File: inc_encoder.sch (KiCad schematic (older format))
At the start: 14 parts, among them U3 AM26LV32xD

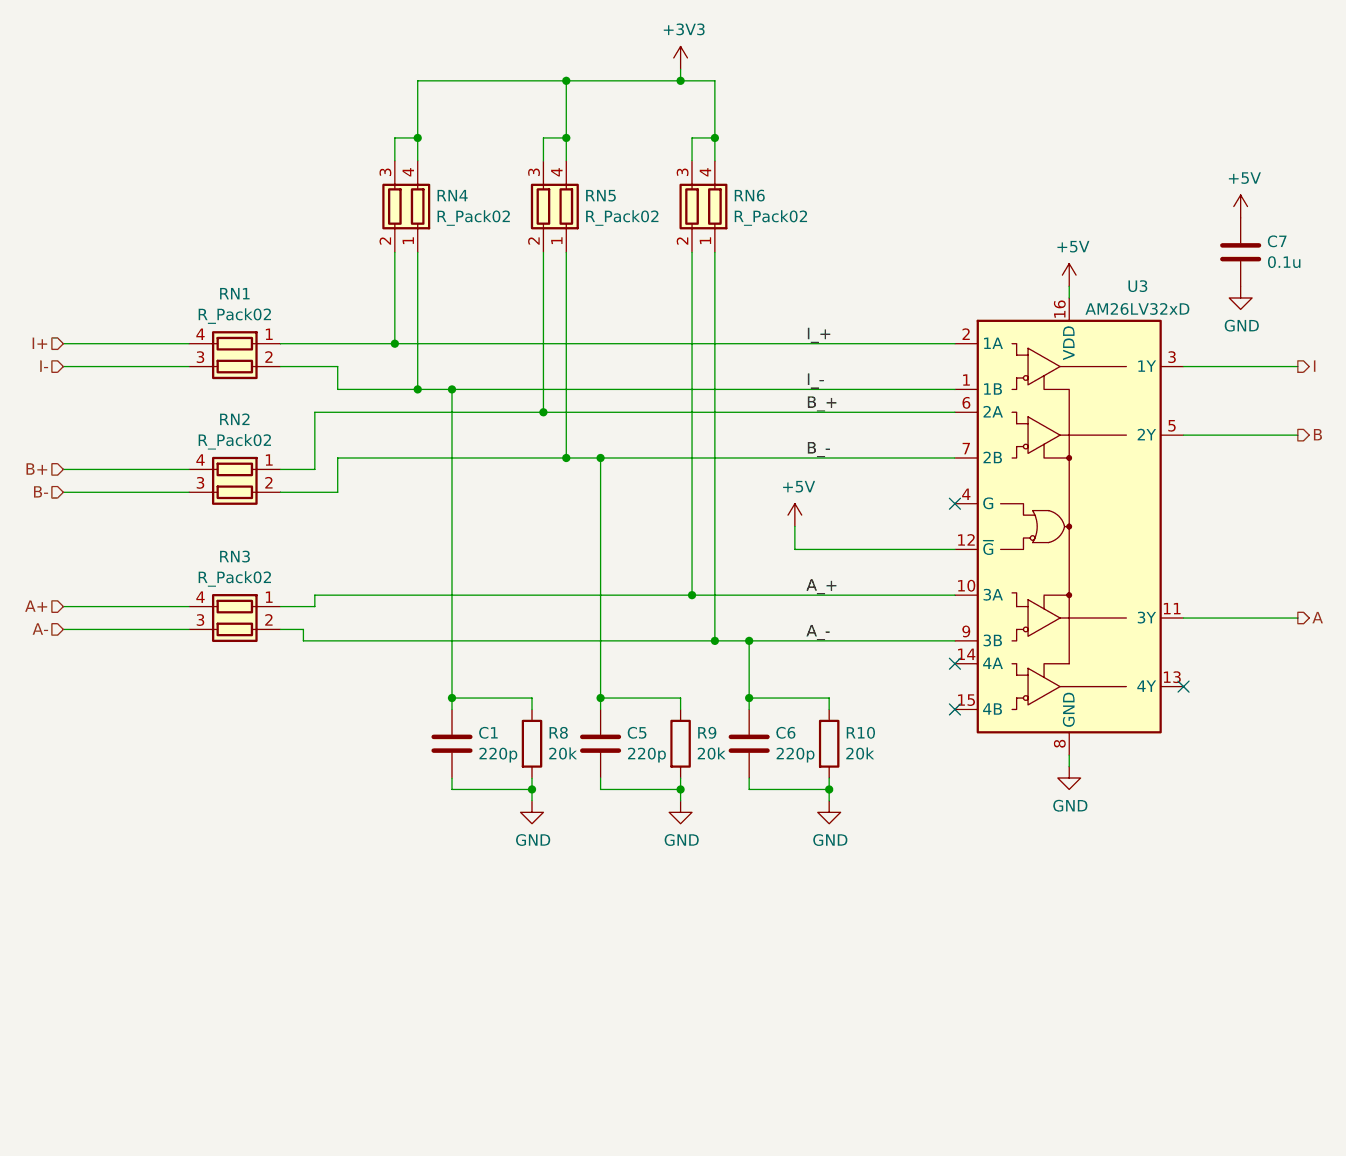
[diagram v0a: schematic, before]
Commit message: 見つけた設計ミスを全部反映
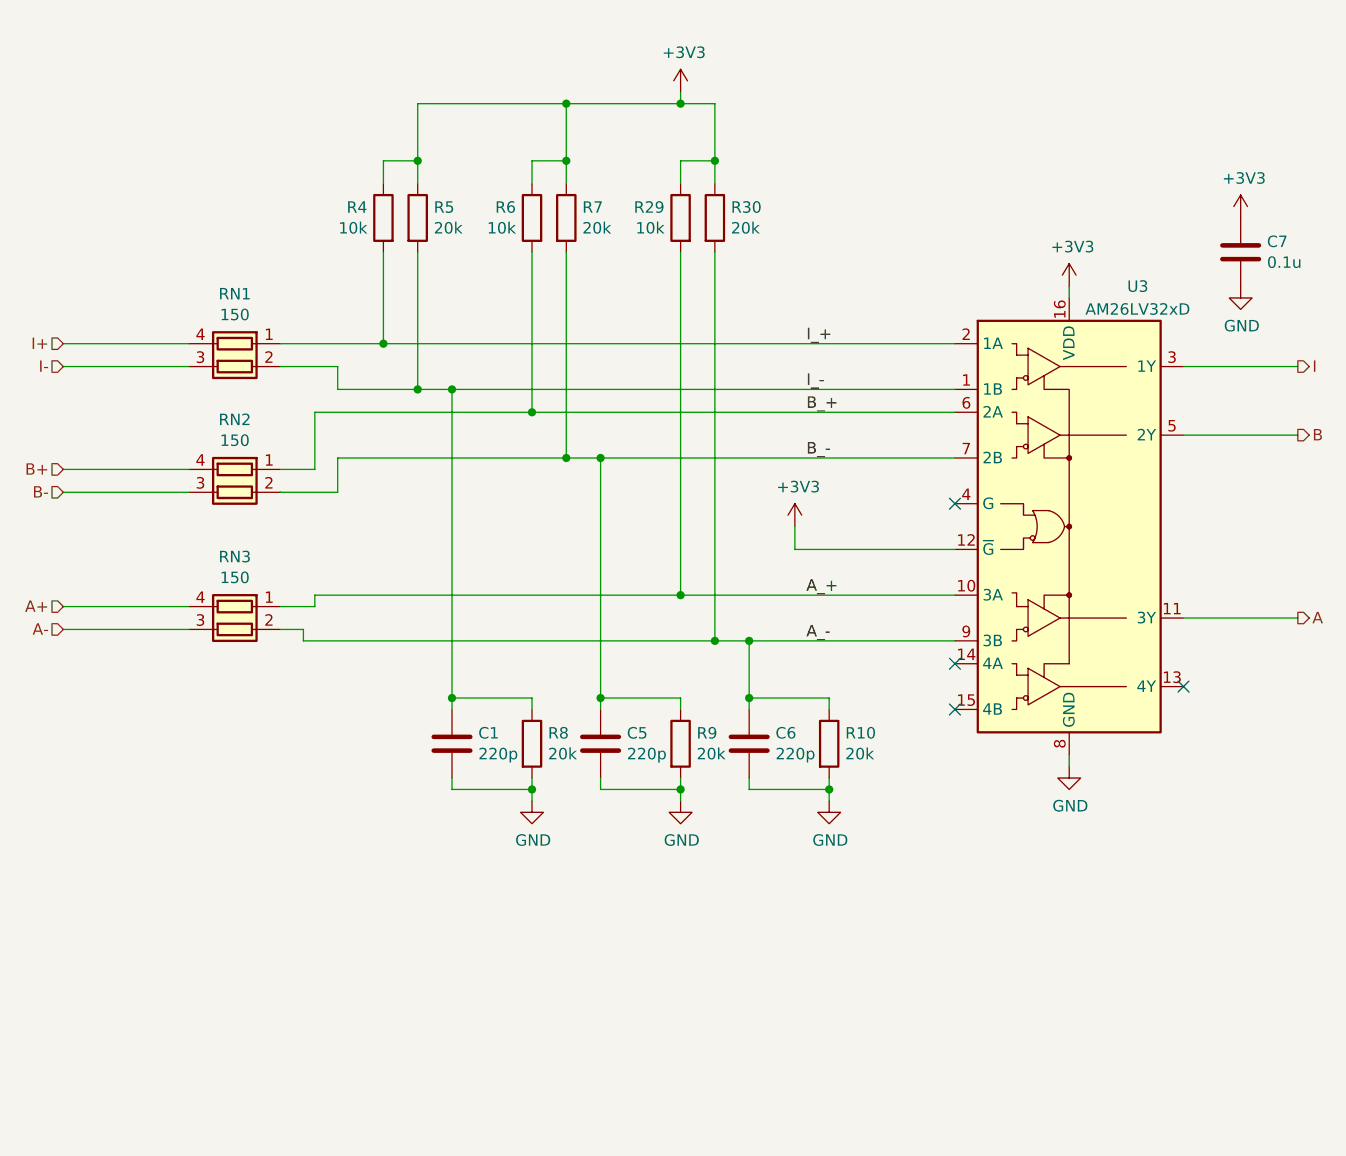
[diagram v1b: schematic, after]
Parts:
- removed RN4, RN5, RN6: R_Pack02, Resistor_SMD:R_Array_Concave_2x0603, symbol Device:R_Pack02
- added R29, R4, R6: 10k, Resistor_SMD:R_0603_1608Metric, symbol Device:R
- added R30, R5, R7: 20k, Resistor_SMD:R_0603_1608Metric, symbol Device:R
- RN1, RN2, RN3: value R_Pack02 -> 150
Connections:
- net +5V is gone; now on net +3V3: C7.1, U3.12 (~G), U3.16 (VDD)
- net +3V3: now also R29.1, R30.1, R4.1, R5.1, R6.1, R7.1
- net A_+: now also R29.2
- net A_-: now also R30.2
- net B_+: now also R6.2
- net B_-: now also R7.2
- net I_+: now also R4.2
- net I_-: now also R5.2
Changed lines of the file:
@@
 EESchema Schematic File Version 4
-LIBS:Encoder_check-cache
 EELAYER 30 0
 EELAYER END
@@
 NoConn ~ 5900 4800
 NoConn ~ 5900 5000
-$Comp
-L power:+5V #PWR?
-U 1 1 5E355A9E
-P 5200 4200
-AR Path="/5E355A9E" Ref="#PWR?"  Part="1"
-AR Path="/5E34E778/5E355A9E" Ref="#PWR0105"  Part="1"
-F 0 "#PWR0105" H 5200 4050 50  0001 C CNN
-F 1 "+5V" H 5215 4373 50  0000 C CNN
-F 2 "" H 5200 4200 50  0001 C CNN
-F 3 "" H 5200 4200 50  0001 C CNN
-	1    5200 4200
-	1    0    0    -1
-$EndComp
 Wire Wire Line
 	5200 4200 5200 4300
 Wire Wire Line
 	5200 4300 5900 4300
-$Comp
-L power:+5V #PWR?
-U 1 1 5E355AA6
-P 6400 3150
-AR Path="/5E355AA6" Ref="#PWR?"  Part="1"
-AR Path="/5E34E778/5E355AA6" Ref="#PWR0106"  Part="1"
-F 0 "#PWR0106" H 6400 3000 50  0001 C CNN
-F 1 "+5V" H 6415 3323 50  0000 C CNN
-F 2 "" H 6400 3150 50  0001 C CNN
-F 3 "" H 6400 3150 50  0001 C CNN
-	1    6400 3150
-	1    0    0    -1
-$EndComp
 Wire Wire Line
 	6400 3150 6400 3200
@@
 $EndComp
 $Comp
-L power:+5V #PWR?
-U 1 1 5E355AB3
-P 7150 2850
-AR Path="/5E355AB3" Ref="#PWR?"  Part="1"
-AR Path="/5E34E778/5E355AB3" Ref="#PWR0107"  Part="1"
-F 0 "#PWR0107" H 7150 2700 50  0001 C CNN
-F 1 "+5V" H 7165 3023 50  0000 C CNN
-F 2 "" H 7150 2850 50  0001 C CNN
-F 3 "" H 7150 2850 50  0001 C CNN
-	1    7150 2850
-	1    0    0    -1
-$EndComp
-$Comp
 L power:GND #PWR?
 U 1 1 5E355AB9
@@
 L power:+3V3 #PWR0122
 U 1 1 5E365891
-P 4700 2200
-F 0 "#PWR0122" H 4700 2050 50  0001 C CNN
-F 1 "+3V3" H 4715 2373 50  0000 C CNN
-F 2 "" H 4700 2200 50  0001 C CNN
-F 3 "" H 4700 2200 50  0001 C CNN
-	1    4700 2200
-	1    0    0    -1
-$EndComp
-Wire Wire Line
-	4700 2200 4700 2250
-Wire Wire Line
-	4700 2250 4850 2250
-Wire Wire Line
-	4850 2250 4850 2500
-Wire Wire Line
-	4750 2600 4750 2500
-Wire Wire Line
-	4750 2500 4850 2500
-Connection ~ 4850 2500
-Wire Wire Line
-	4850 2500 4850 2600
-Wire Wire Line
-	4700 2250 4200 2250
-Wire Wire Line
-	4200 2250 4200 2500
-Connection ~ 4700 2250
-Wire Wire Line
-	4200 2500 4100 2500
-Connection ~ 4200 2500
-Wire Wire Line
-	4200 2500 4200 2600
-Wire Wire Line
-	4100 2600 4100 2500
+P 4700 2300
+F 0 "#PWR0122" H 4700 2150 50  0001 C CNN
+F 1 "+3V3" H 4715 2473 50  0000 C CNN
+F 2 "" H 4700 2300 50  0001 C CNN
+F 3 "" H 4700 2300 50  0001 C CNN
+	1    4700 2300
+	1    0    0    -1
+$EndComp
+Wire Wire Line
+	4700 2300 4700 2350
+Wire Wire Line
+	4700 2350 4850 2350
+Wire Wire Line
+	4850 2350 4850 2600
+Wire Wire Line
+	4700 2700 4700 2600
+Wire Wire Line
+	4700 2600 4850 2600
+Connection ~ 4850 2600
+Wire Wire Line
+	4850 2600 4850 2700
+Wire Wire Line
+	4700 2350 4200 2350
+Wire Wire Line
+	4200 2350 4200 2600
+Connection ~ 4700 2350
+Wire Wire Line
+	4200 2600 4050 2600
+Connection ~ 4200 2600
+Wire Wire Line
+	4200 2600 4200 2700
+Wire Wire Line
+	4050 2700 4050 2600
 $Comp
 L Device:R R10
@@
 	4350 3900 5900 3900
 Wire Wire Line
-	2950 3400 3450 3400
+	2950 3400 3400 3400
 Wire Wire Line
 	3700 3600 3550 3600
 Wire Wire Line
-	3100 3700 4100 3700
-Wire Wire Line
-	3450 3000 3450 3400
-Connection ~ 3450 3400
-Wire Wire Line
-	3450 3400 5900 3400
+	3100 3700 4050 3700
+Wire Wire Line
+	3400 3000 3400 3400
+Connection ~ 3400 3400
+Wire Wire Line
+	3400 3400 5900 3400
 Wire Wire Line
 	3550 3000 3550 3600
 Connection ~ 3550 3600
 Wire Wire Line
-	4100 3000 4100 3700
-Connection ~ 4100 3700
-Wire Wire Line
-	4100 3700 5900 3700
+	4050 3000 4050 3700
+Connection ~ 4050 3700
+Wire Wire Line
+	4050 3700 5900 3700
 Wire Wire Line
 	4200 3000 4200 3900
@@
 Wire Wire Line
 	3100 4550 3100 4500
-$Comp
-L Device:R_Pack02 RN6
-U 1 1 5E4869DA
-P 4750 2800
-F 0 "RN6" H 4570 2846 50  0000 R CNN
-F 1 "R_Pack02" H 4570 2755 50  0000 R CNN
-F 2 "Resistor_SMD:R_Array_Concave_2x0603" V 4925 2800 50  0001 C CNN
-F 3 "~" H 4750 2800 50  0001 C CNN
-	1    4750 2800
-	-1   0    0    -1
-$EndComp
 $Comp
 L Device:R_Pack02 RN3
@@
 P 2750 4650
 F 0 "RN3" V 2433 4650 50  0000 C CNN
-F 1 "R_Pack02" V 2524 4650 50  0000 C CNN
+F 1 "150" V 2524 4650 50  0000 C CNN
 F 2 "Resistor_SMD:R_Array_Concave_2x0603" V 2925 4650 50  0001 C CNN
 F 3 "~" H 2750 4650 50  0001 C CNN
@@
 	0    -1   1    0
 $EndComp
-$Comp
-L Device:R_Pack02 RN5
-U 1 1 5E48D078
-P 4100 2800
-F 0 "RN5" H 3920 2846 50  0000 R CNN
-F 1 "R_Pack02" H 3920 2755 50  0000 R CNN
-F 2 "Resistor_SMD:R_Array_Concave_2x0603" V 4275 2800 50  0001 C CNN
-F 3 "~" H 4100 2800 50  0001 C CNN
-	1    4100 2800
-	-1   0    0    -1
-$EndComp
-$Comp
-L Device:R_Pack02 RN4
-U 1 1 5E48D4FD
-P 3450 2800
-F 0 "RN4" H 3270 2846 50  0000 R CNN
-F 1 "R_Pack02" H 3270 2755 50  0000 R CNN
-F 2 "Resistor_SMD:R_Array_Concave_2x0603" V 3625 2800 50  0001 C CNN
-F 3 "~" H 3450 2800 50  0001 C CNN
-	1    3450 2800
-	-1   0    0    -1
-$EndComp
-Wire Wire Line
-	3450 2600 3450 2500
-Wire Wire Line
-	3450 2500 3550 2500
-Wire Wire Line
-	3550 2500 3550 2600
-Wire Wire Line
-	3550 2500 3550 2250
-Wire Wire Line
-	3550 2250 4200 2250
-Connection ~ 3550 2500
-Connection ~ 4200 2250
+Wire Wire Line
+	3400 2700 3400 2600
+Wire Wire Line
+	3400 2600 3550 2600
+Wire Wire Line
+	3550 2600 3550 2700
+Wire Wire Line
+	3550 2600 3550 2350
+Wire Wire Line
+	3550 2350 4200 2350
+Connection ~ 3550 2600
+Connection ~ 4200 2350
 Wire Wire Line
 	3700 3600 5900 3600
@@
 P 2750 3500
 F 0 "RN1" V 2433 3500 50  0000 C CNN
-F 1 "R_Pack02" V 2524 3500 50  0000 C CNN
+F 1 "150" V 2524 3500 50  0000 C CNN
 F 2 "Resistor_SMD:R_Array_Concave_2x0603" V 2925 3500 50  0001 C CNN
 F 3 "~" H 2750 3500 50  0001 C CNN
@@
 P 2750 4050
 F 0 "RN2" V 2433 4050 50  0000 C CNN
-F 1 "R_Pack02" V 2524 4050 50  0000 C CNN
+F 1 "150" V 2524 4050 50  0000 C CNN
 F 2 "Resistor_SMD:R_Array_Concave_2x0603" V 2925 4050 50  0001 C CNN
 F 3 "~" H 2750 4050 50  0001 C CNN
@@
 	3050 4700 4850 4700
 Wire Wire Line
-	3100 4500 4750 4500
-Wire Wire Line
-	4750 3000 4750 4500
-Connection ~ 4750 4500
-Wire Wire Line
-	4750 4500 5900 4500
+	3100 4500 4700 4500
+Wire Wire Line
+	4700 3000 4700 4500
+Connection ~ 4700 4500
+Wire Wire Line
+	4700 4500 5900 4500
 Wire Wire Line
 	4850 3000 4850 4700
@@
 Text Label 5250 3400 0    50   ~ 0
 I_+
+$Comp
+L Device:R R30
+U 1 1 5E55B2E2
+P 4850 2850
+F 0 "R30" H 4920 2896 50  0000 L CNN
+F 1 "20k" H 4920 2805 50  0000 L CNN
+F 2 "Resistor_SMD:R_0603_1608Metric" V 4780 2850 50  0001 C CNN
+F 3 "~" H 4850 2850 50  0001 C CNN
+	1    4850 2850
+	1    0    0    -1
+$EndComp
+$Comp
+L Device:R R7
+U 1 1 5E55BC17
+P 4200 2850
+F 0 "R7" H 4270 2896 50  0000 L CNN
+F 1 "20k" H 4270 2805 50  0000 L CNN
+F 2 "Resistor_SMD:R_0603_1608Metric" V 4130 2850 50  0001 C CNN
+F 3 "~" H 4200 2850 50  0001 C CNN
+	1    4200 2850
+	1    0    0    -1
+$EndComp
+$Comp
+L Device:R R5
+U 1 1 5E55BEC8
+P 3550 2850
+F 0 "R5" H 3620 2896 50  0000 L CNN
+F 1 "20k" H 3620 2805 50  0000 L CNN
+F 2 "Resistor_SMD:R_0603_1608Metric" V 3480 2850 50  0001 C CNN
+F 3 "~" H 3550 2850 50  0001 C CNN
+	1    3550 2850
+	1    0    0    -1
+$EndComp
+$Comp
+L Device:R R29
+U 1 1 5E55C33C
+P 4700 2850
+F 0 "R29" H 4770 2896 50  0000 L CNN
+F 1 "10k" H 4770 2805 50  0000 L CNN
+F 2 "Resistor_SMD:R_0603_1608Metric" V 4630 2850 50  0001 C CNN
+F 3 "~" H 4700 2850 50  0001 C CNN
+	1    4700 2850
+	-1   0    0    -1
+$EndComp
+$Comp
+L Device:R R6
+U 1 1 5E55C54C
+P 4050 2850
+F 0 "R6" H 4120 2896 50  0000 L CNN
+F 1 "10k" H 4120 2805 50  0000 L CNN
+F 2 "Resistor_SMD:R_0603_1608Metric" V 3980 2850 50  0001 C CNN
+F 3 "~" H 4050 2850 50  0001 C CNN
+	1    4050 2850
+	-1   0    0    -1
+$EndComp
+$Comp
+L Device:R R4
+U 1 1 5E55CA6D
+P 3400 2850
+F 0 "R4" H 3470 2896 50  0000 L CNN
+F 1 "10k" H 3470 2805 50  0000 L CNN
+F 2 "Resistor_SMD:R_0603_1608Metric" V 3330 2850 50  0001 C CNN
+F 3 "~" H 3400 2850 50  0001 C CNN
+	1    3400 2850
+	-1   0    0    -1
+$EndComp
+$Comp
+L power:+3V3 #PWR0109
+U 1 1 5E575986
+P 6400 3150
+F 0 "#PWR0109" H 6400 3000 50  0001 C CNN
+F 1 "+3V3" H 6415 3323 50  0000 C CNN
+F 2 "" H 6400 3150 50  0001 C CNN
+F 3 "" H 6400 3150 50  0001 C CNN
+	1    6400 3150
+	1    0    0    -1
+$EndComp
+$Comp
+L power:+3V3 #PWR0112
+U 1 1 5E575EB5
+P 7150 2850
+F 0 "#PWR0112" H 7150 2700 50  0001 C CNN
+F 1 "+3V3" H 7165 3023 50  0000 C CNN
+F 2 "" H 7150 2850 50  0001 C CNN
+F 3 "" H 7150 2850 50  0001 C CNN
+	1    7150 2850
+	1    0    0    -1
+$EndComp
+$Comp
+L power:+3V3 #PWR0143
+U 1 1 5E660EAB
+P 5200 4200
+F 0 "#PWR0143" H 5200 4050 50  0001 C CNN
+F 1 "+3V3" H 5215 4373 50  0000 C CNN
+F 2 "" H 5200 4200 50  0001 C CNN
+F 3 "" H 5200 4200 50  0001 C CNN
+	1    5200 4200
+	1    0    0    -1
+$EndComp
 $EndSCHEMATC

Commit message: エンコーダの配線ミスってた
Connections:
- net B: now also U3.13 (4Y); no longer U3.5 (2Y)
- net B+: now also RN2.3 (R2.2); no longer RN2.4 (R1.2)
- net B-: now also RN2.4 (R1.2); no longer RN2.3 (R2.2)
- net B_+: now also RN2.2 (R2.1), U3.14 (4A); no longer RN2.1 (R1.1), U3.6 (2A)
- net B_-: now also RN2.1 (R1.1), U3.15 (4B); no longer RN2.2 (R2.1), U3.7 (2B)
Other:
- moved on the sheet: C1, C5, C6, R10, R8, R9

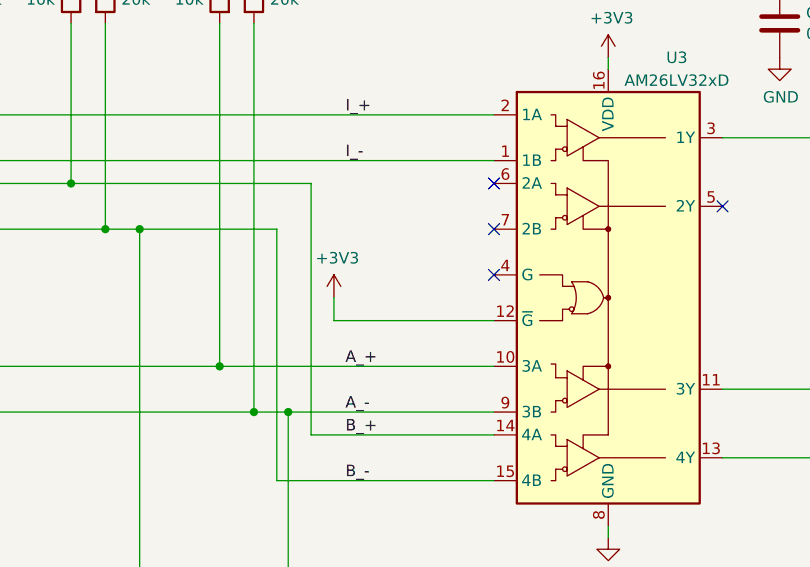
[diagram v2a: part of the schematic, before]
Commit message: レシーバの出力が有効になっていないとうアホなミスを修正
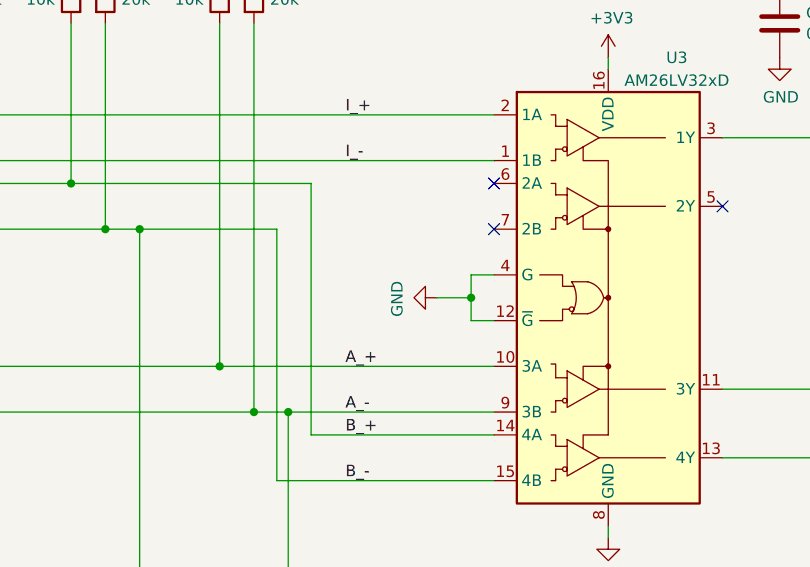
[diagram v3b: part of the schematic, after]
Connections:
- net +3V3: no longer U3.12 (~G)
- net GND: now also U3.12 (~G), U3.4 (G)
- no-connect marks 4 -> 3
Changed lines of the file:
@@
 NoConn ~ 5900 3700
-Wire Wire Line
-	5200 4200 5200 4300
-Wire Wire Line
-	5200 4300 5900 4300
 Wire Wire Line
 	6400 3150 6400 3200
@@
 Text Label 5250 4700 0    50   ~ 0
 A_-
-NoConn ~ 5900 4100
 Text Label 5250 3400 0    50   ~ 0
 I_+
@@
 	1    0    0    -1
 $EndComp
-$Comp
-L power:+3V3 #PWR0143
-U 1 1 5E660EAB
-P 5200 4200
-F 0 "#PWR0143" H 5200 4050 50  0001 C CNN
-F 1 "+3V3" H 5215 4373 50  0000 C CNN
-F 2 "" H 5200 4200 50  0001 C CNN
-F 3 "" H 5200 4200 50  0001 C CNN
-	1    5200 4200
-	1    0    0    -1
-$EndComp
 Wire Wire Line
 	3050 4700 4850 4700
@@
 	0    -1   1    0
 $EndComp
+$Comp
+L power:GND #PWR?
+U 1 1 5E8287B2
+P 5650 4200
+AR Path="/5E8287B2" Ref="#PWR?"  Part="1"
+AR Path="/5E34E778/5E8287B2" Ref="#PWR0115"  Part="1"
+F 0 "#PWR0115" H 5650 3950 50  0001 C CNN
+F 1 "GND" H 5655 4027 50  0000 C CNN
+F 2 "" H 5650 4200 50  0001 C CNN
+F 3 "" H 5650 4200 50  0001 C CNN
+	1    5650 4200
+	0    1    1    0
+$EndComp
+Wire Wire Line
+	5900 4100 5800 4100
+Wire Wire Line
+	5800 4100 5800 4200
+Wire Wire Line
+	5800 4300 5900 4300
+Wire Wire Line
+	5650 4200 5800 4200
+Connection ~ 5800 4200
+Wire Wire Line
+	5800 4200 5800 4300
 $EndSCHEMATC
